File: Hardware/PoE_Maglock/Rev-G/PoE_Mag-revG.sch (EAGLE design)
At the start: 89 parts, among them IC2 ATMEGA32U4-MU, J11 1X2-3.5MM, J14 1X2-3.5MM, J15 1X2-3.5MM, J16 1X2-3.5MM, J17 1X2-3.5MM, J2 1X2-3.5MM, J3 1X2-3.5MM, J4 1X2-3.5MM, J5 1X2-3.5MM, J6 10103594-0001LF, Q1 35A/25V/8.5mΩ, Q3 35A/25V/8.5mΩ, Q5 35A/25V/8.5mΩ, Q6 35A/25V/8.5mΩ, SW1 SPST_TACT-KMR2, U4 W5500, X2 J1011FHY931147C, Y4 8MHz

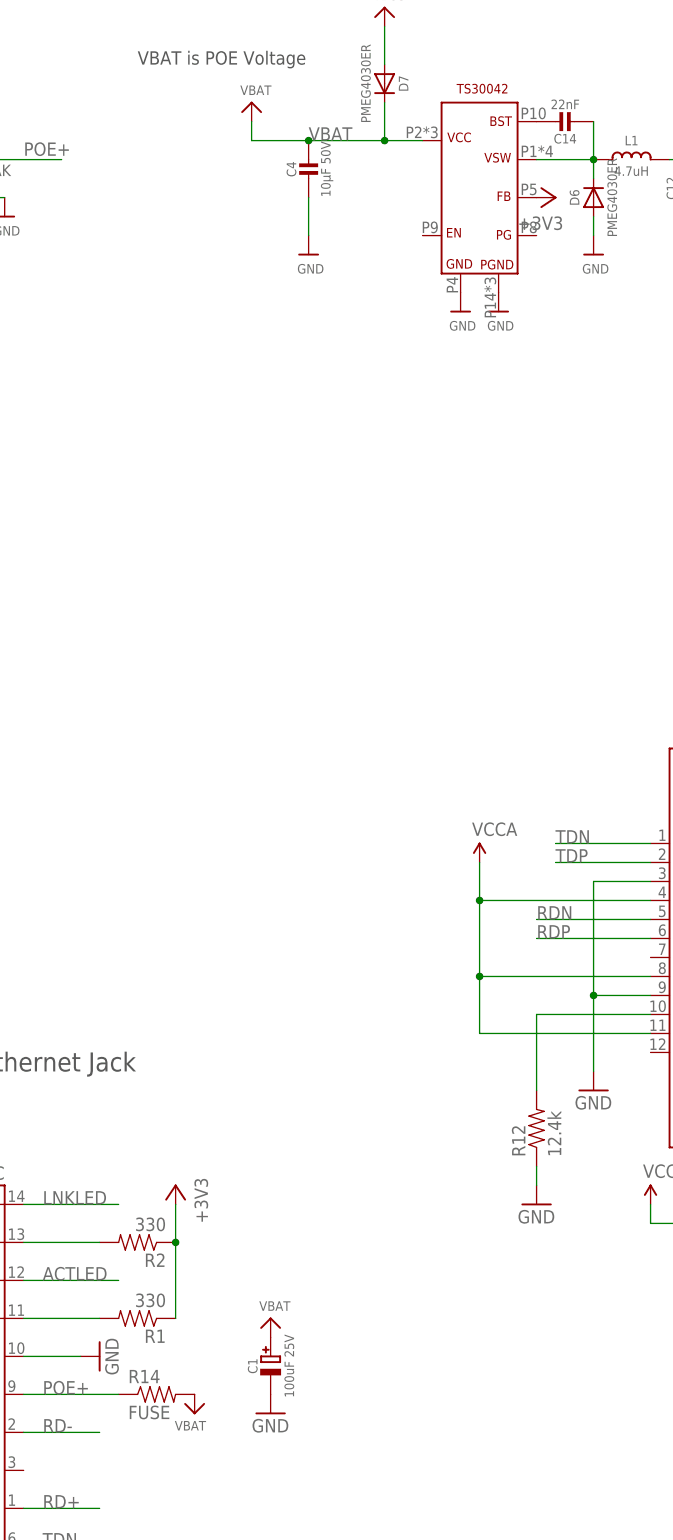
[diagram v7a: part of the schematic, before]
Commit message: HEEP-1046 dylan approved, init bom csv
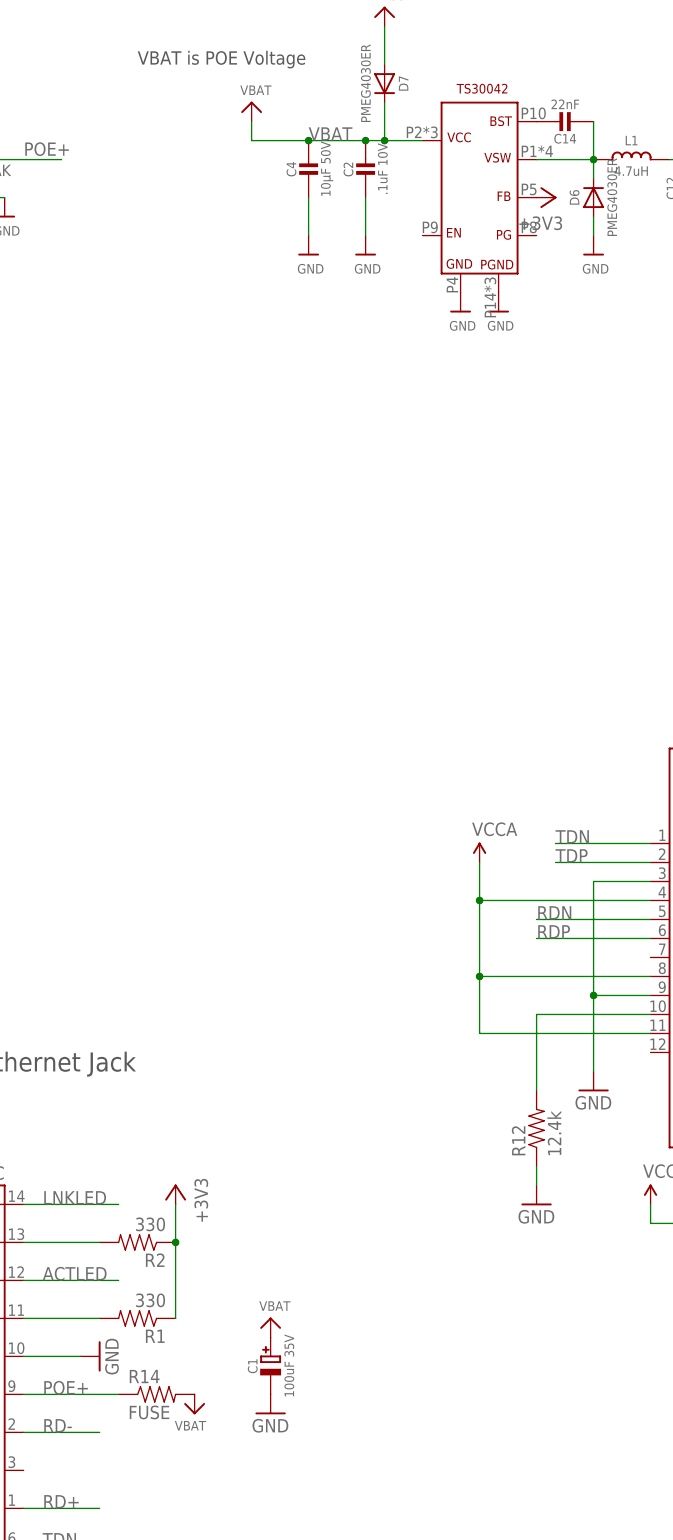
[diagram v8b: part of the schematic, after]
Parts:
- added C2: .1uF 10V, microbuilder:CAP_CERAMIC0603MINI
- C1: value 100uF 25V -> 100uF 35V
- C12, C13: device microbuilder:CAP_CERAMIC0603MINI -> microbuilder:CAP_CERAMIC0805-NOOUTLINE
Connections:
- net GND: now also C2.2
- net VBAT: now also C2.1
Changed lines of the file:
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@@
 <grid distance="0.1" unitdist="inch" unit="inch" style="lines" multiple="1" display="no" altdistance="0.01" altunitdist="inch" altunit="inch"/>
 <layers>
-<layer number="1" name="Top" color="4" fill="1" visible="no" active="no"/>
-<layer number="16" name="Bottom" color="1" fill="1" visible="no" active="no"/>
-<layer number="17" name="Pads" color="2" fill="1" visible="no" active="no"/>
-<layer number="18" name="Vias" color="2" fill="1" visible="no" active="no"/>
-<layer number="19" name="Unrouted" color="15" fill="1" visible="no" active="no"/>
-<layer number="20" name="Dimension" color="24" fill="1" visible="no" active="no"/>
-<layer number="21" name="tPlace" color="14" fill="1" visible="no" active="no"/>
-<layer number="22" name="bPlace" color="7" fill="1" visible="no" active="no"/>
-<layer number="23" name="tOrigins" color="15" fill="1" visible="no" active="no"/>
-<layer number="24" name="bOrigins" color="15" fill="1" visible="no" active="no"/>
-<layer number="25" name="tNames" color="7" fill="1" visible="no" active="no"/>
-<layer number="26" name="bNames" color="7" fill="1" visible="no" active="no"/>
-<layer number="27" name="tValues" color="15" fill="1" visible="no" active="no"/>
-<layer number="28" name="bValues" color="7" fill="1" visible="no" active="no"/>
+<layer number="1" name="Top" color="4" fill="1" visible="yes" active="no"/>
+<layer number="16" name="Bottom" color="1" fill="1" visible="yes" active="no"/>
+<layer number="17" name="Pads" color="2" fill="1" visible="yes" active="no"/>
+<layer number="18" name="Vias" color="2" fill="1" visible="yes" active="no"/>
+<layer number="19" name="Unrouted" color="15" fill="1" visible="yes" active="no"/>
+<layer number="20" name="Dimension" color="24" fill="1" visible="yes" active="no"/>
+<layer number="21" name="tPlace" color="14" fill="1" visible="yes" active="no"/>
+<layer number="22" name="bPlace" color="7" fill="1" visible="yes" active="no"/>
+<layer number="23" name="tOrigins" color="15" fill="1" visible="yes" active="no"/>
+<layer number="24" name="bOrigins" color="15" fill="1" visible="yes" active="no"/>
+<layer number="25" name="tNames" color="7" fill="1" visible="yes" active="no"/>
+<layer number="26" name="bNames" color="7" fill="1" visible="yes" active="no"/>
+<layer number="27" name="tValues" color="15" fill="1" visible="yes" active="no"/>
+<layer number="28" name="bValues" color="7" fill="1" visible="yes" active="no"/>
 <layer number="29" name="tStop" color="7" fill="3" visible="no" active="no"/>
 <layer number="30" name="bStop" color="7" fill="6" visible="no" active="no"/>
@@
 <layer number="35" name="tGlue" color="7" fill="4" visible="no" active="no"/>
 <layer number="36" name="bGlue" color="7" fill="5" visible="no" active="no"/>
-<layer number="37" name="tTest" color="7" fill="1" visible="no" active="no"/>
-<layer number="38" name="bTest" color="7" fill="1" visible="no" active="no"/>
+<layer number="37" name="tTest" color="7" fill="1" visible="yes" active="no"/>
+<layer number="38" name="bTest" color="7" fill="1" visible="yes" active="no"/>
 <layer number="39" name="tKeepout" color="4" fill="11" visible="no" active="no"/>
 <layer number="40" name="bKeepout" color="1" fill="11" visible="no" active="no"/>
@@
 <layer number="44" name="Drills" color="7" fill="1" visible="no" active="no"/>
 <layer number="45" name="Holes" color="7" fill="1" visible="no" active="no"/>
-<layer number="46" name="Milling" color="3" fill="1" visible="no" active="no"/>
-<layer number="47" name="Measures" color="7" fill="1" visible="no" active="no"/>
-<layer number="48" name="Document" color="7" fill="1" visible="no" active="no"/>
-<layer number="49" name="Reference" color="7" fill="1" visible="no" active="no"/>
-<layer number="50" name="dxf" color="7" fill="1" visible="no" active="no"/>
-<layer number="51" name="tDocu" color="7" fill="1" visible="no" active="no"/>
-<layer number="52" name="bDocu" color="7" fill="1" visible="no" active="no"/>
-<layer number="53" name="tGND_GNDA" color="7" fill="9" visible="no" active="no"/>
-<layer number="54" name="bGND_GNDA" color="1" fill="9" visible="no" active="no"/>
-<layer number="56" name="wert" color="7" fill="1" visible="no" active="no"/>
-<layer number="57" name="tCAD" color="7" fill="1" visible="no" active="no"/>
-<layer number="59" name="tCarbon" color="7" fill="1" visible="no" active="no"/>
-<layer number="60" name="bCarbon" color="7" fill="1" visible="no" active="no"/>
+<layer number="46" name="Milling" color="3" fill="1" visible="yes" active="no"/>
+<layer number="47" name="Measures" color="7" fill="1" visible="yes" active="no"/>
+<layer number="48" name="Document" color="7" fill="1" visible="yes" active="no"/>
+<layer number="49" name="Reference" color="7" fill="1" visible="yes" active="no"/>
+<layer number="50" name="dxf" color="7" fill="1" visible="yes" active="no"/>
+<layer number="51" name="tDocu" color="7" fill="1" visible="yes" active="no"/>
+<layer number="52" name="bDocu" color="7" fill="1" visible="yes" active="no"/>
+<layer number="53" name="tGND_GNDA" color="7" fill="9" visible="yes" active="no"/>
+<layer number="54" name="bGND_GNDA" color="1" fill="9" visible="yes" active="no"/>
+<layer number="56" name="wert" color="7" fill="1" visible="yes" active="no"/>
+<layer number="57" name="tCAD" color="7" fill="1" visible="yes" active="no"/>
+<layer number="59" name="tCarbon" color="7" fill="1" visible="yes" active="no"/>
+<layer number="60" name="bCarbon" color="7" fill="1" visible="yes" active="no"/>
 <layer number="90" name="Modules" color="5" fill="1" visible="yes" active="yes"/>
 <layer number="91" name="Nets" color="2" fill="1" visible="yes" active="yes"/>
@@
 <part name="U$22" library="microbuilder" deviceset="GND" device=""/>
 <part name="U$23" library="microbuilder" deviceset="GND" device=""/>
-<part name="C12" library="microbuilder" deviceset="CAP_CERAMIC" device="0603MINI" value="22uF 10V"/>
-<part name="C13" library="microbuilder" deviceset="CAP_CERAMIC" device="0603MINI" value="22uF 10V"/>
+<part name="C12" library="microbuilder" deviceset="CAP_CERAMIC" device="0805-NOOUTLINE" value="22uF 10V"/>
+<part name="C13" library="microbuilder" deviceset="CAP_CERAMIC" device="0805-NOOUTLINE" value="22uF 10V"/>
 <part name="L1" library="microbuilder" deviceset="INDUCTOR" device="TDK_VLC5045" value="4.7uH"/>
 <part name="C14" library="microbuilder" deviceset="CAP_CERAMIC" device="0603MINI" value="22nF"/>
@@
 <part name="U$26" library="microbuilder" deviceset="VBUS" device=""/>
 <part name="GND18" library="SparkFun-Aesthetics" deviceset="GND" device=""/>
-<part name="C1" library="microbuilder" deviceset="CAP_ELECTROLYTIC" device="PANASONIC_D" value="100uF 25V"/>
+<part name="C1" library="microbuilder" deviceset="CAP_ELECTROLYTIC" device="PANASONIC_D" value="100uF 35V"/>
 <part name="U$2" library="microbuilder" deviceset="VBAT" device=""/>
 <part name="GND24" library="SparkFun-Aesthetics" deviceset="GND" device=""/>
@@
 <part name="GND10" library="supply1" deviceset="GND" device=""/>
 <part name="U$4" library="microbuilder" deviceset="VBAT" device=""/>
+<part name="C2" library="microbuilder" deviceset="CAP_CERAMIC" device="0603MINI" value=".1uF 10V"/>
+<part name="U$16" library="microbuilder" deviceset="GND" device=""/>
 </parts>
 <sheets>
@@
 <instance part="GND10" gate="1" x="452.12" y="307.34" rot="R180"/>
 <instance part="U$4" gate="G$1" x="452.12" y="289.56" rot="R180"/>
+<instance part="C2" gate="G$1" x="91.44" y="223.52"/>
+<instance part="U$16" gate="G$1" x="91.44" y="213.36"/>
 </instances>
 <busses>
@@
 <pinref part="GND10" gate="1" pin="GND"/>
 </segment>
+<segment>
+<pinref part="C2" gate="G$1" pin="2"/>
+<pinref part="U$16" gate="G$1" pin="GND"/>
+<wire x1="91.44" y1="215.9" x2="91.44" y2="220.98" width="0.1524" layer="91"/>
+</segment>
 </net>
 <net name="RD-" class="0">
@@
 <wire x1="76.2" y1="228.6" x2="83.82" y2="228.6" width="0.1524" layer="91"/>
 <pinref part="C4" gate="G$1" pin="1"/>
-<wire x1="83.82" y1="228.6" x2="93.98" y2="228.6" width="0.1524" layer="91"/>
+<wire x1="83.82" y1="228.6" x2="91.44" y2="228.6" width="0.1524" layer="91"/>
 <junction x="83.82" y="228.6"/>
 <pinref part="U$19" gate="G$1" pin="VCC"/>
 <pinref part="D7" gate="G$1" pin="C"/>
+<wire x1="91.44" y1="228.6" x2="93.98" y2="228.6" width="0.1524" layer="91"/>
 <wire x1="93.98" y1="228.6" x2="99.06" y2="228.6" width="0.1524" layer="91"/>
 <wire x1="93.98" y1="233.68" x2="93.98" y2="228.6" width="0.1524" layer="91"/>
 <junction x="93.98" y="228.6"/>
-</segment>
-<segment>
+<pinref part="C2" gate="G$1" pin="1"/>
+<junction x="91.44" y="228.6"/>
+</segment>
+<segment>
